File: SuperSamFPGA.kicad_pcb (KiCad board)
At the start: 6 copper layers, 63.2 x 82.3 mm, 102 parts, among them J1 DataBus, J2 Video, J3 AddressBus, J4 ControlOut, J5 ControlIn, J6 JTAG, SW1 Tactile, U10 TXS0108EPW, U11 TXS0104EPW, U12 TXS0104EPW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

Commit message: complete initial design
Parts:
- added J7: BusService, Connector_PinHeader_2.54mm:PinHeader_1x10_P2.54mm_Vertical, B.Cu at (162.9, 133.3)
- added J8: RomAddr, Connector_PinHeader_2.54mm:PinHeader_1x08_P2.54mm_Vertical, B.Cu at (178.7, 70.2)
- added U1: 74LVC573, Package_SO:TSSOP-20_4.4x6.5mm_P0.65mm, F.Cu at (127.4, 114.2)
- C26, C27: footprint Capacitor_SMD:C_0402_1005Metric -> Capacitor_SMD:C_0805_2012Metric
- J6: moved to B.Cu
- moved C17 3.18 mm to (170.2, 69.5)
- moved C19 3.18 mm to (161.5, 75.2)
- moved C20 3.18 mm to (161.9, 69.5)
- moved U11 3.18 mm to (173.1, 72.8)
- moved U12 3.18 mm to (165.0, 72.8)
- moved C16 3.15 mm to (169.7, 75.2)
- moved J6 1.87 mm to (178.7, 95.6), turned to 180 degrees
- moved C8 1.79 mm to (159.6, 94.4)
- moved R1 0.88 mm to (167.3, 103.6), turned to 90 degrees
- moved C27 0.50 mm to (137.3, 68.6)
- moved C39 0.47 mm to (174.0, 113.5)
- moved C26 0.45 mm to (127.3, 68.6)
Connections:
- U2 pad A12: unconnected-(U2A-IO_L7N_T1_AD2N_15-PadA12) -> /A2
- U2 pad A13: /A2 -> /A6
- U2 pad A14: /A6 -> /A7
- U2 pad B11: unconnected-(U2A-IO_L4N_T0_15-PadB11) -> /A0
- U2 pad B12: unconnected-(U2A-IO_L7P_T1_AD2P_15-PadB12) -> /A3
- U2 pad B14: /A7 -> /A8
- U2 pad B15: /A9 -> /A11
- U2 pad B16: /A12 -> /A13
- U2 pad C12: unconnected-(U2A-IO_L6N_T0_VREF_15-PadC12) -> /A1
- U2 pad C13: /A3 -> /A5
- U2 pad C14: /A5 -> /A9
- U2 pad C16: /A11 -> /CSS
- U2 pad C17: /A13 -> /~{RST}
- U2 pad C18: /CSS -> /~{A}/G
- U2 pad D11: unconnected-(U2A-IO_L6P_T0_15-PadD11) -> GND
- U2 pad D13: /A1 -> unconnected-(U2A-IO_L11P_T1_SRCC_15-PadD13)
- U2 pad D15: /A8 -> /A12
- U2 pad D16: /~{RST} -> /R/~{W}
- U2 pad D18: /~{A}/G -> /GM1
- U2 pad E13: /A0 -> unconnected-(U2A-IO_L12P_T1_MRCC_15-PadE13)
- U2 pad E15: /R/~{W} -> unconnected-(U2A-IO_L13P_T2_MRCC_15-PadE15)
- U2 pad E17: /GM1 -> /GM2
- U2 pad E18: /GM2 -> /E
- U2 pad F17: /E -> /S0
- U2 pad G14: unconnected-(U2A-IO_L22P_T3_A17_15-PadG14) -> /RZ16
- U2 pad G15: /S0 -> /RZ13
- U2 pad H14: unconnected-(U2A-IO_25_15-PadH14) -> /RZ18
- U2 pad H16: unconnected-(U2A-IO_L20P_T3_A20_15-PadH16) -> /RZ14
- U2 pad H17: unconnected-(U2A-IO_L23P_T3_FOE_B_15-PadH17) -> /RZ17
- U2 pad H18: unconnected-(U2A-IO_L23N_T3_FWE_B_15-PadH18) -> /RZ15
- U2 pad J18: unconnected-(U2A-IO_L3P_T0_DQS_PUDC_B_14-PadJ18) -> /~{RWE}
- U2 pad K18: unconnected-(U2A-IO_L3N_T0_DQS_EMCCLK_14-PadK18) -> /~{ROE}
- U2 pad L18: unconnected-(U2A-IO_L4N_T0_D05_14-PadL18) -> /~{NMI}
- U2 pad M15: unconnected-(U2A-IO_L6N_T0_D08_VREF_14-PadM15) -> /~{IRQ}
- U2 pad M16: unconnected-(U2A-IO_L7P_T1_D09_14-PadM16) -> /~{FIRQ}
- U2 pad N14: unconnected-(U2A-IO_L8N_T1_D12_14-PadN14) -> /BA
- U2 pad N16: unconnected-(U2A-IO_L9P_T1_DQS_14-PadN16) -> /BS
- U2 pad P15: unconnected-(U2A-IO_L11P_T1_SRCC_14-PadP15) -> /HALT
- U2 pad P16: unconnected-(U2A-IO_L11N_T1_SRCC_14-PadP16) -> /LIC
- U2 pad R15: unconnected-(U2A-IO_L12N_T1_MRCC_14-PadR15) -> /TSC
- U2 pad R16: unconnected-(U2A-IO_L14P_T2_SRCC_14-PadR16) -> /AVMA
- U2 pad V4: unconnected-(U2B-IO_L18N_T2_34-PadV4) -> /RLE
- U9 pad 24: /RD6 -> /CC6
- U9 pad 28: /RD5 -> /CC5
- U9 pad 29: /RD4 -> /CC4
- U9 pad 4: /RD3 -> /CC3
- U9 pad 5: /RD2 -> /CC2
- U9 pad 6: /RD1 -> /CC1
- U9 pad 7: /RD0 -> /CC0
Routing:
- net /AVMA: track 0.00 -> 45.8 mm, vias 0 -> 1
- net /LIC: track 0.00 -> 45.0 mm, vias 0 -> 1
- net /BA: track 0.00 -> 44.8 mm, vias 0 -> 2
- net /TSC: track 0.00 -> 44.7 mm, vias 0 -> 2
- net /HALT: track 0.00 -> 44.7 mm, vias 0 -> 2
- net /~{IRQ}: track 0.00 -> 43.2 mm, vias 0 -> 2
- net /BS: track 0.00 -> 42.6 mm, vias 0 -> 1
- net /~{FIRQ}: track 0.00 -> 41.9 mm, vias 0 -> 1
- net /~{NMI}: track 0.00 -> 39.8 mm, vias 0 -> 1
- net /RZ13: track 0.00 -> 36.1 mm, vias 0 -> 1
- net /RZ14: track 0.00 -> 33.1 mm, vias 0 -> 1
- net /RZ16: track 0.00 -> 31.7 mm, vias 0 -> 1
- net /RLE: track 0.00 -> 31.7 mm, vias 0 -> 2
- net /CC2: track 0.00 -> 29.8 mm
- net /RZ15: track 0.00 -> 29.0 mm, vias 0 -> 1
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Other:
- board text added: "+"
- board text added: "ADDRESS"
- board text added: "BLUE"
- board text added: "BUS CONTROL"
- board text added: "C"
- board text added: "CHAR DATA"
- board text added: "FORMAT"
- board text added: "GREEN"
- board text added: "I"
- board text added: "JTAG"
- board text added: "M"
- board text added: "MEMORY AND DATA"
- board text added: "O"
- board text added: "RED"
- board text added: "ROM CONTROL"
- board text added: "VIDEO"
- board text removed: "chroma"
- board text removed: "composite"
- board text removed: "luma"

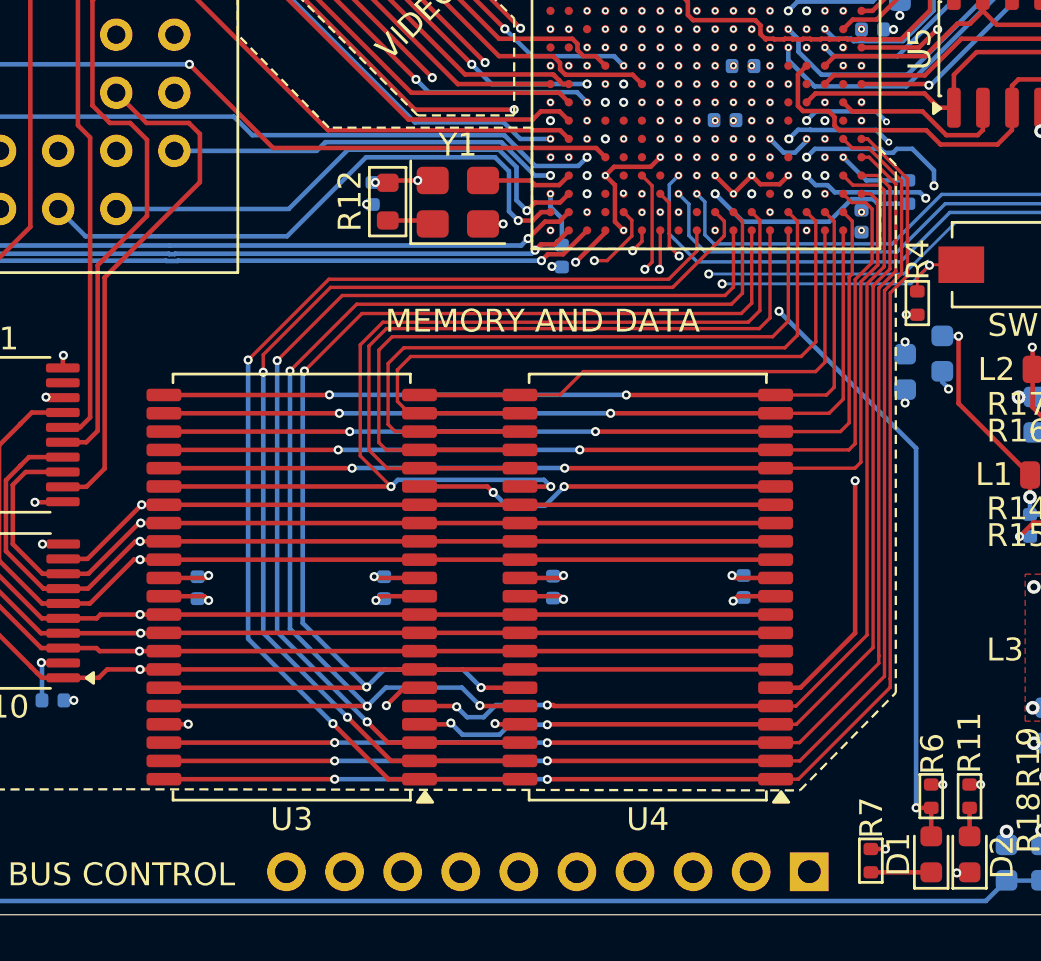
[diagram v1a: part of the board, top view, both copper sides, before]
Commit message: implement alternative sram
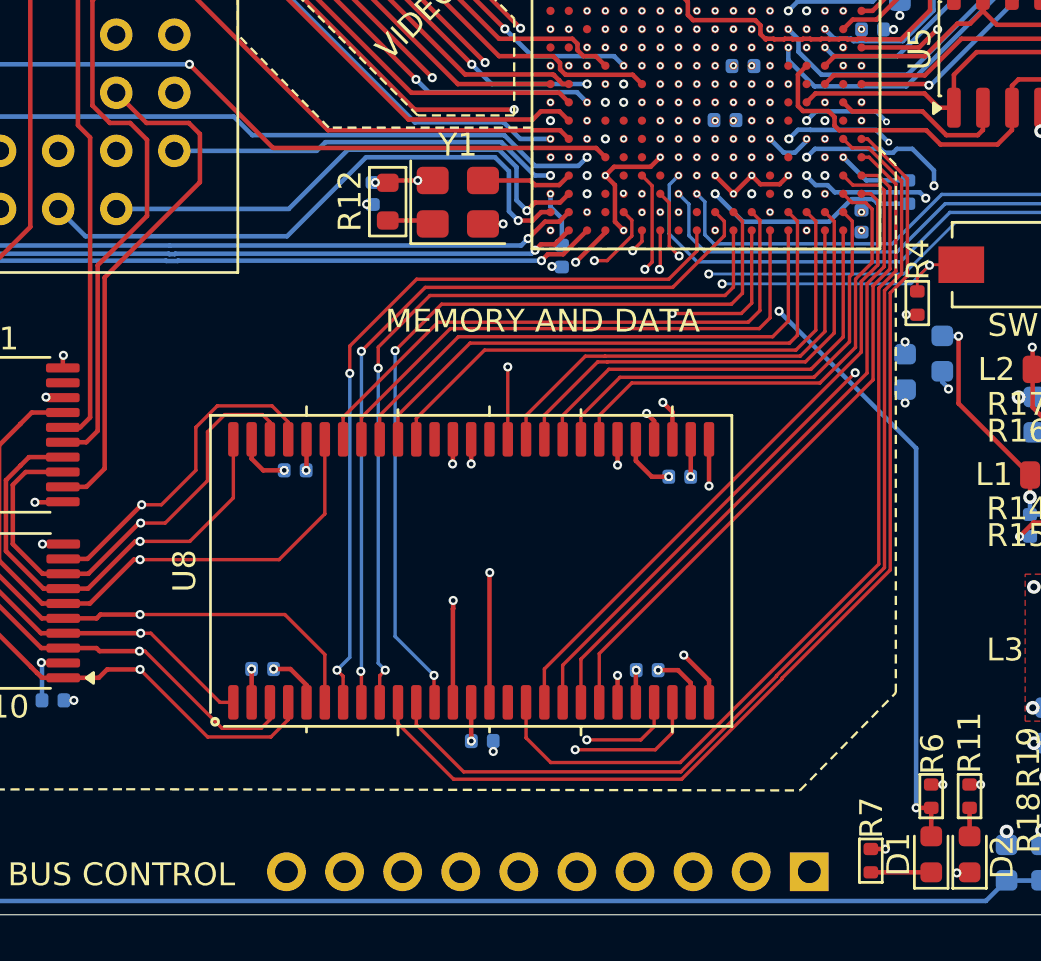
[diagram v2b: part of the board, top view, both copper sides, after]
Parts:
- removed U3, U4: IS61WV51216BLL, Package_SO:TSOP-II-44_10.16x18.41mm_P0.8mm
- added C23: 100nF, Capacitor_SMD:C_0402_1005Metric, B.Cu at (148.6, 127.6)
- added U8: CY7C10612G30-10ZSXI, PCM_Package_SO_AKL:TSOP-II-54_22.2x10.16mm_P0.8mm, F.Cu at (148.2, 120.1)
- moved C21 6.67 mm to (140.5, 115.7), turned to 180 degrees
- moved C22 6.39 mm to (139.0, 124.4), turned to 0 degrees
- moved C12 5.55 mm to (157.3, 116.0), turned to 180 degrees
- moved C15 5.49 mm to (155.9, 124.5), turned to 0 degrees
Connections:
- U2 pad T14: /~{CE}1 -> /~{CE}
- U2 pad T15: /~{CE}2 -> /Z20
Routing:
- net /Z0: track 55.2 -> 18.2 mm, vias 3 -> 2
- net /~{CE}: track 0.00 -> 33.2 mm, vias 0 -> 2
- net /~{CE}1: track 32.1 -> 0.00 mm, vias 2 -> 0
- net /Z20: track 0.00 -> 28.4 mm, vias 0 -> 2
- net /~{CE}2: track 24.6 -> 0.00 mm, vias 2 -> 0
- net /Z19: track 47.8 -> 25.6 mm, vias 2 -> 0
- net /~{Z0}: track 57.2 -> 36.0 mm, vias 3 -> 2
- net /Z14: track 42.4 -> 21.4 mm, vias 2 -> 0
- net /Z13: track 39.6 -> 20.0 mm, vias 2 -> 0
- net /Z12: track 37.3 -> 19.4 mm, vias 2 -> 0
- net /Z11: track 37.3 -> 20.7 mm, vias 2 -> 0
- net /Z16: track 56.0 -> 39.9 mm, vias 2 -> 0
- net /Z1: track 49.1 -> 33.7 mm
- net /Z2: track 49.2 -> 34.5 mm
- net /Z15: track 43.2 -> 28.8 mm, vias 2 -> 0
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
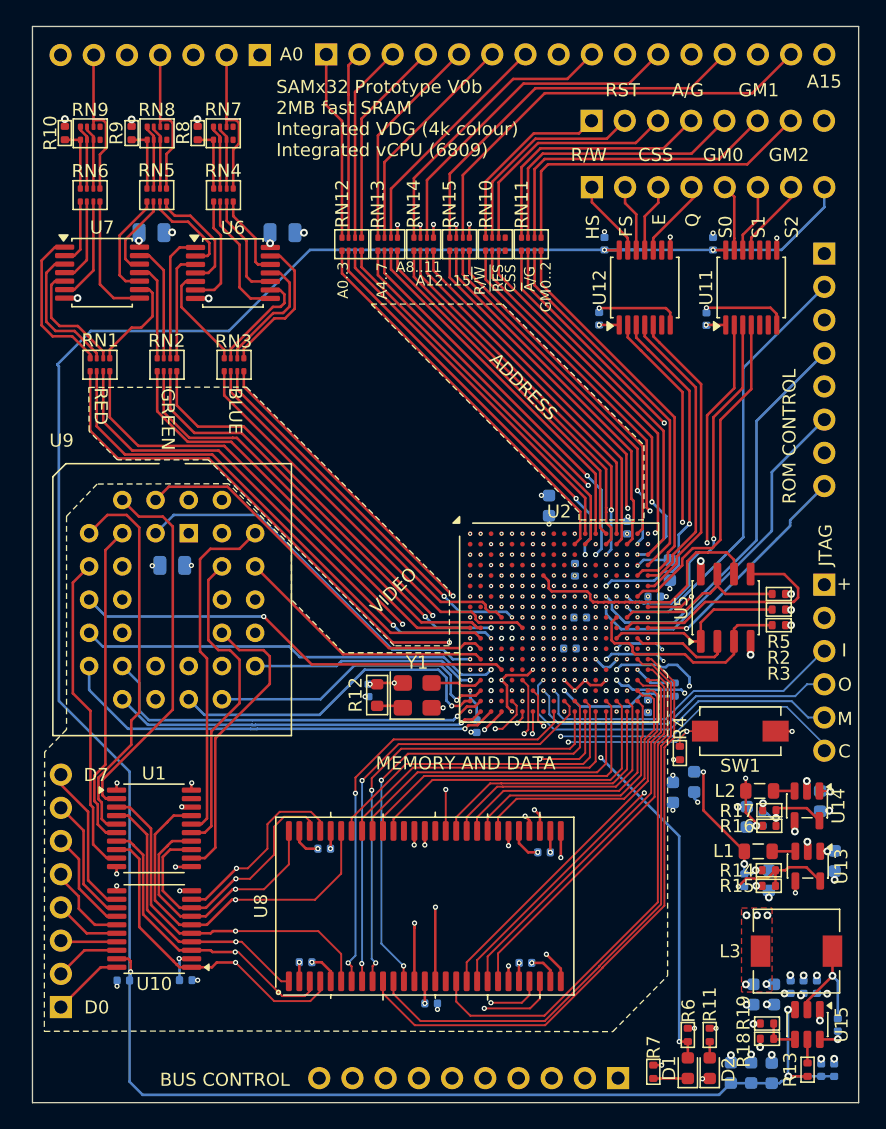
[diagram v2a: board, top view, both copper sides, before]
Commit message: switch to single chip dac
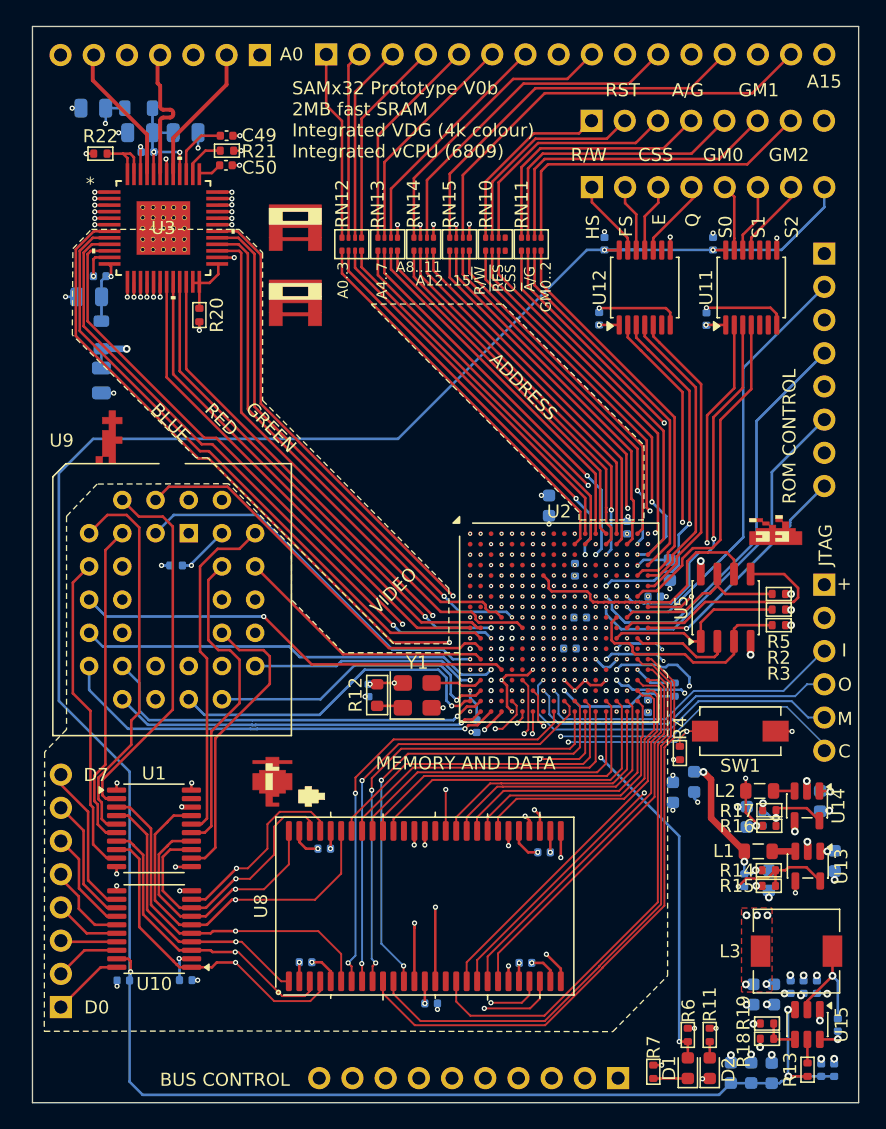
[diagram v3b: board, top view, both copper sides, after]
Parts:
- removed R10, R8, R9: 470R, PCM_Resistor_SMD_AKL:R_0402_1005Metric
- removed RN1, RN2, RN3: 33R, PCM_Resistor_SMD_AKL:R_Array_Convex_4x0402
- removed RN4, RN5, RN6: 470R, PCM_Resistor_SMD_AKL:R_Array_Convex_4x0402
- removed RN7, RN8, RN9: 220R, PCM_Resistor_SMD_AKL:R_Array_Convex_4x0402
- removed U6, U7: SN74AC17PWR, Package_SO:TSSOP-14_4.4x5mm_P0.65mm
- added C24: 10uF, Capacitor_SMD:C_0805_2012Metric, B.Cu at (123.4, 79.9)
- added C28: 10uF, Capacitor_SMD:C_0805_2012Metric, B.Cu at (122.5, 73.5)
- added C46: 100nF, Capacitor_SMD:C_0402_1005Metric, B.Cu at (129.1, 94.1)
- added C47: 100nF, Capacitor_SMD:C_0402_1005Metric, B.Cu at (123.3, 72.0)
- added C48: 100nF, Capacitor_SMD:C_0402_1005Metric, B.Cu at (126.9, 62.5)
- added C49: 100nF, Capacitor_SMD:C_0402_1005Metric, F.Cu at (133.0, 61.2)
- added C50: 100nF, Capacitor_SMD:C_0402_1005Metric, F.Cu at (132.9, 63.5)
- added L4: 4.7uH, Inductor_SMD:L_0805_2012Metric, B.Cu at (123.4, 76.5)
- added L5: 4.7uH, Inductor_SMD:L_0805_2012Metric, B.Cu at (126.3, 59.1)
- added R20: 2.2K, PCM_Resistor_SMD_AKL:R_0402_1005Metric, F.Cu at (130.9, 74.9)
- added R21: 3.8K, PCM_Resistor_SMD_AKL:R_0402_1005Metric, F.Cu at (133.0, 62.4)
- added R22: 2.2K, PCM_Resistor_SMD_AKL:R_0402_1005Metric, F.Cu at (123.3, 62.6)
- added U3: THS8136IPHP, Library:PHP48_4P1X4P1, F.Cu at (128.2, 68.3)
- C26, C27: value 100uF -> 10uF
- moved C18 33.2 mm to (126.4, 61.0)
- moved C27 10.6 mm to (129.9, 61.0)
- moved C26 10.5 mm to (122.8, 59.1), turned to 180 degrees
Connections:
- C18 pad 1: +3V3 -> /AVDD
- C27 pad 1: +3V3 -> /AVDD
- J2 pad 2: /BLUE -> /GREEN
- J2 pad 4: /GREEN -> /RED
- J2 pad 6: /RED -> /BLUE
- U2 pad J4: /B1 -> /G2
- U2 pad J5: /B3 -> /G1
- U2 pad J6: /B2 -> /G0
- U2 pad K1: /G1 -> /R0
- U2 pad K2: /G0 -> /R1
- U2 pad K3: /G2 -> /R2
- U2 pad K5: /G3 -> /R3
- U2 pad K6: /B0 -> /G3
- U2 pad L2: /R2 -> /B1
- U2 pad L3: /R0 -> /B2
- U2 pad L4: /R1 -> /B3
- U2 pad L5: /Format -> /VCLK
- U2 pad M4: unconnected-(U2B-IO_L10P_T1_34-PadM4) -> /Format
- U2 pad N4: /R3 -> /B0
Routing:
- net +1V8: track 43.4 -> 113.4 mm, vias 11 -> 13
- net /VCLK: track 0.00 -> 42.9 mm, vias 0 -> 2
- net GND: track 58.4 -> 84.4 mm, vias 157 -> 179
- net /B0: track 32.2 -> 52.5 mm, vias 0 -> 2
- net /B1: track 29.6 -> 49.1 mm
- net /B2: track 29.8 -> 48.8 mm
- net /B3: track 29.6 -> 48.5 mm
- net Net-(RN1-R4.1): track 12.1 -> 0.00 mm
- net Net-(RN3-R1.1): track 11.1 -> 0.00 mm
- net Net-(RN1-R3.1): track 10.6 -> 0.00 mm
- net /AVDD: track 0.00 -> 10.2 mm, vias 0 -> 2
- net Net-(RN2-R2.1): track 9.98 -> 0.00 mm
- net Net-(RN4-R3.2): track 9.89 -> 0.00 mm
- net Net-(RN6-R1.2): track 9.79 -> 0.00 mm
- net Net-(RN3-R2.1): track 9.67 -> 0.00 mm
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
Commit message: production ready
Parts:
- removed C12: 100nF, Capacitor_SMD:C_0402_1005Metric
- removed U8: CY7C10612G30-10ZSXI, PCM_Package_SO_AKL:TSOP-II-54_22.2x10.16mm_P0.8mm
- added U4: IS61WV102416BLL-10TLI, Package_SO:TSOP-I-48_18.4x12mm_P0.5mm, F.Cu at (146.7, 120.8)
- moved C23 11.4 mm to (157.8, 120.8), turned to 90 degrees
- moved C21 5.44 mm to (138.3, 120.8), turned to -90 degrees
- moved C22 5.00 mm to (135.7, 120.8), turned to -90 degrees
- moved C15 3.81 mm to (155.1, 120.8), turned to 90 degrees
- moved C50 1.09 mm to (132.9, 62.4)
- moved C49 1.09 mm to (133.0, 60.1)
- moved R21 1.09 mm to (133.0, 61.3)
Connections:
- U2 pad T12: /~{WE} -> /~{CE}
- U2 pad T14: /~{CE} -> /~{WE}
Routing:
- net /Z11: track 20.7 -> 43.0 mm, vias 0 -> 2
- net /Z10: track 20.1 -> 41.4 mm, vias 0 -> 2
- net /~{Z0}: track 36.0 -> 17.0 mm
- net /RD4: track 92.9 -> 75.3 mm, vias 3 -> 2
- net /Z9: track 25.3 -> 41.6 mm, vias 0 -> 2
- net /Z8: track 25.5 -> 40.7 mm, vias 0 -> 2
- net /RD3: track 91.3 -> 76.3 mm, vias 3 -> 2
- net /Z18: track 47.4 -> 32.8 mm
- net /Z7: track 24.6 -> 38.6 mm, vias 0 -> 2
- net /Z17: track 46.5 -> 32.6 mm
- net /RD7: track 74.6 -> 61.0 mm, vias 3 -> 2
- net /RD0: track 90.9 -> 78.6 mm, vias 3 -> 2
- net /RD6: track 80.6 -> 68.5 mm, vias 3 -> 2
- net /RD1: track 87.9 -> 77.4 mm, vias 3 -> 2
- net /Z15: track 28.8 -> 19.0 mm
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
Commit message: refine design
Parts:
- removed J8: RomAddr, Connector_PinHeader_2.54mm:PinHeader_1x08_P2.54mm_Vertical
- added U6: SST39LF040-55, PCM_Package_LCC_AKL:PLCC-32_THT-Socket, F.Cu at (141.2, 76.6)
- moved RN13 6.75 mm to (145.3, 62.8)
- moved RN12 6.75 mm to (142.6, 62.8)
- moved C20 5.30 mm to (167.1, 70.2)
- moved C19 5.30 mm to (166.7, 76.0)
- moved U12 5.30 mm to (170.2, 73.6)
- moved C16 4.14 mm to (173.8, 76.0)
- moved U11 4.13 mm to (177.2, 73.6)
- moved C17 4.13 mm to (174.3, 70.2)
- moved RN10 2.64 mm to (153.6, 66.9)
- moved RN11 2.64 mm to (156.3, 66.9)
- moved RN14 2.64 mm to (148.1, 66.9)
- moved RN15 2.64 mm to (150.8, 66.9)
- moved U9 1.55 mm to (128.9, 92.6)
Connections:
- J7 pad 10: GND -> /BUSY
- U2 pad G14: /RZ16 -> ~{RWE}
- U2 pad H14: /RZ18 -> /RZ14
- U2 pad H16: /RZ14 -> ~{ROE}
- U2 pad J18: /~{RWE} -> /RZ16
- U2 pad K18: /~{ROE} -> /RZ18
- U2 pad P14: unconnected-(U2A-IO_L12P_T1_MRCC_14-PadP14) -> /BUSY
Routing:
- net /RD7: track 61.0 -> 163.5 mm, vias 2 -> 3
- net /RD6: track 68.5 -> 166.2 mm, vias 2 -> 3
- net /RD5: track 69.4 -> 160.9 mm, vias 2 -> 3
- net /RD4: track 75.3 -> 165.5 mm, vias 2 -> 3
- net /RD3: track 76.3 -> 158.3 mm, vias 2 -> 3
- net /RD2: track 76.1 -> 152.3 mm, vias 2 -> 3
- net /RD1: track 77.4 -> 153.1 mm, vias 2 -> 3
- net /RD0: track 78.6 -> 147.4 mm, vias 2 -> 3
- net ~{RWE}: track 0.00 -> 56.0 mm, vias 0 -> 1
- net /BUSY: track 0.00 -> 54.4 mm, vias 0 -> 1
- net ~{ROE}: track 0.00 -> 43.8 mm, vias 0 -> 1
- net /A2: track 28.9 -> 65.8 mm, vias 0 -> 1
- net /A3: track 29.9 -> 66.7 mm, vias 0 -> 1
- net /A4: track 31.3 -> 64.8 mm, vias 2 -> 3
- net /A5: track 30.3 -> 63.5 mm, vias 2 -> 3
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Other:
- board size 63.2 x 82.3 mm -> 63.7 x 82.3 mm
- board text removed: "ROM CONTROL"
